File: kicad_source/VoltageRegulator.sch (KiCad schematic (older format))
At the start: 27 parts, among them P2 WR-TBL_691313710002, Q1 IPD90P03P4L- 04, U9 IFX91041EJV

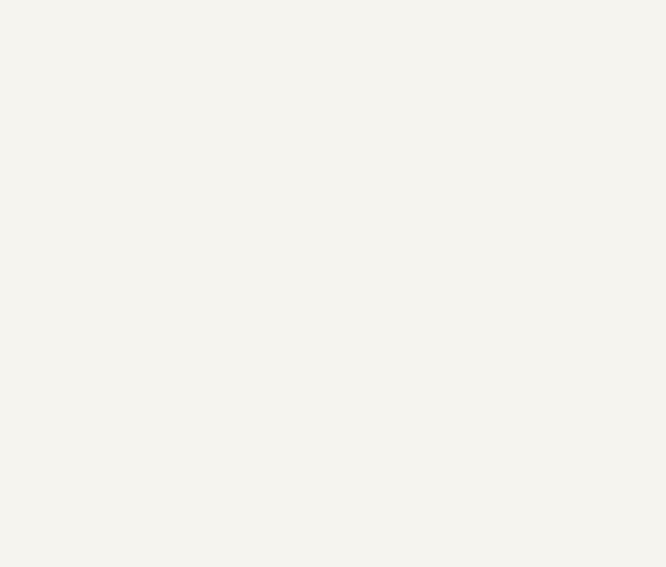
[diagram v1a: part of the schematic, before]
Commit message: added most missing 3d models, changed mounting holes to parts and generated step model
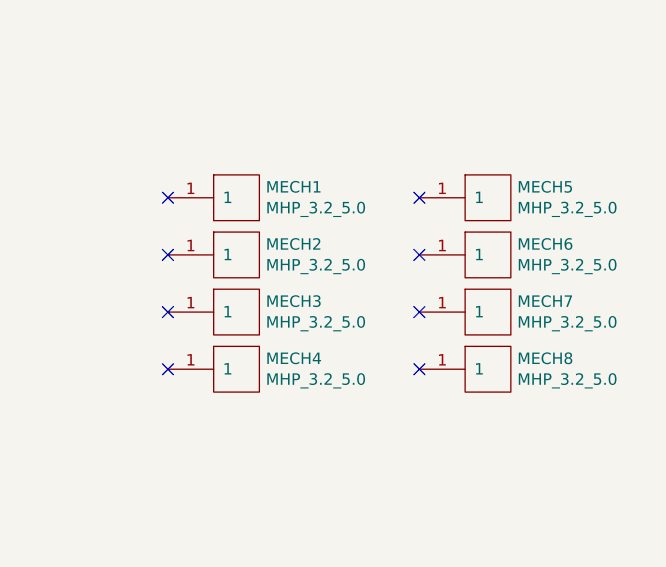
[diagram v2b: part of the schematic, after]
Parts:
- added MECH1, MECH2, MECH3, MECH4, MECH5, MECH6, MECH7, MECH8: MHP_3.2_5.0, MECH_mounting_holes:MHP_3.2_5.0, symbol MECH_mounting-holes:MHP_3.2_5.0
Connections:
- no-connect marks 0 -> 8
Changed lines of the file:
@@
 Text Label 4550 6450 0    60   ~ 0
 VIN_UNPOL
+$Comp
+L MECH_mounting-holes:MHP_3.2_5.0 MECH1
+U 1 1 5E994B25
+P 8550 5300
+F 0 "MECH1" H 8678 5346 50  0000 L CNN
+F 1 "MHP_3.2_5.0" H 8678 5255 50  0000 L CNN
+F 2 "MECH_mounting_holes:MHP_3.2_5.0" H 8450 5350 50  0001 C CNN
+F 3 "" H 8550 5300 50  0001 C CNN
+	1    8550 5300
+	1    0    0    -1
+$EndComp
+$Comp
+L MECH_mounting-holes:MHP_3.2_5.0 MECH2
+U 1 1 5E995892
+P 8550 5550
+F 0 "MECH2" H 8678 5596 50  0000 L CNN
+F 1 "MHP_3.2_5.0" H 8678 5505 50  0000 L CNN
+F 2 "MECH_mounting_holes:MHP_3.2_5.0" H 8450 5600 50  0001 C CNN
+F 3 "" H 8550 5550 50  0001 C CNN
+	1    8550 5550
+	1    0    0    -1
+$EndComp
+$Comp
+L MECH_mounting-holes:MHP_3.2_5.0 MECH3
+U 1 1 5E99663D
+P 8550 5800
+F 0 "MECH3" H 8678 5846 50  0000 L CNN
+F 1 "MHP_3.2_5.0" H 8678 5755 50  0000 L CNN
+F 2 "MECH_mounting_holes:MHP_3.2_5.0" H 8450 5850 50  0001 C CNN
+F 3 "" H 8550 5800 50  0001 C CNN
+	1    8550 5800
+	1    0    0    -1
+$EndComp
+$Comp
+L MECH_mounting-holes:MHP_3.2_5.0 MECH4
+U 1 1 5E996647
+P 8550 6050
+F 0 "MECH4" H 8678 6096 50  0000 L CNN
+F 1 "MHP_3.2_5.0" H 8678 6005 50  0000 L CNN
+F 2 "MECH_mounting_holes:MHP_3.2_5.0" H 8450 6100 50  0001 C CNN
+F 3 "" H 8550 6050 50  0001 C CNN
+	1    8550 6050
+	1    0    0    -1
+$EndComp
+NoConn ~ 8250 5300
+NoConn ~ 8250 5550
+NoConn ~ 8250 5800
+NoConn ~ 8250 6050
+$Comp
+L MECH_mounting-holes:MHP_3.2_5.0 MECH5
+U 1 1 5E9A368E
+P 9650 5300
+F 0 "MECH5" H 9778 5346 50  0000 L CNN
+F 1 "MHP_3.2_5.0" H 9778 5255 50  0000 L CNN
+F 2 "MECH_mounting_holes:MHP_3.2_5.0" H 9550 5350 50  0001 C CNN
+F 3 "" H 9650 5300 50  0001 C CNN
+	1    9650 5300
+	1    0    0    -1
+$EndComp
+$Comp
+L MECH_mounting-holes:MHP_3.2_5.0 MECH6
+U 1 1 5E9A3698
+P 9650 5550
+F 0 "MECH6" H 9778 5596 50  0000 L CNN
+F 1 "MHP_3.2_5.0" H 9778 5505 50  0000 L CNN
+F 2 "MECH_mounting_holes:MHP_3.2_5.0" H 9550 5600 50  0001 C CNN
+F 3 "" H 9650 5550 50  0001 C CNN
+	1    9650 5550
+	1    0    0    -1
+$EndComp
+$Comp
+L MECH_mounting-holes:MHP_3.2_5.0 MECH7
+U 1 1 5E9A36A2
+P 9650 5800
+F 0 "MECH7" H 9778 5846 50  0000 L CNN
+F 1 "MHP_3.2_5.0" H 9778 5755 50  0000 L CNN
+F 2 "MECH_mounting_holes:MHP_3.2_5.0" H 9550 5850 50  0001 C CNN
+F 3 "" H 9650 5800 50  0001 C CNN
+	1    9650 5800
+	1    0    0    -1
+$EndComp
+$Comp
+L MECH_mounting-holes:MHP_3.2_5.0 MECH8
+U 1 1 5E9A36AC
+P 9650 6050
+F 0 "MECH8" H 9778 6096 50  0000 L CNN
+F 1 "MHP_3.2_5.0" H 9778 6005 50  0000 L CNN
+F 2 "MECH_mounting_holes:MHP_3.2_5.0" H 9550 6100 50  0001 C CNN
+F 3 "" H 9650 6050 50  0001 C CNN
+	1    9650 6050
+	1    0    0    -1
+$EndComp
+NoConn ~ 9350 5300
+NoConn ~ 9350 5550
+NoConn ~ 9350 5800
+NoConn ~ 9350 6050
 $EndSCHEMATC

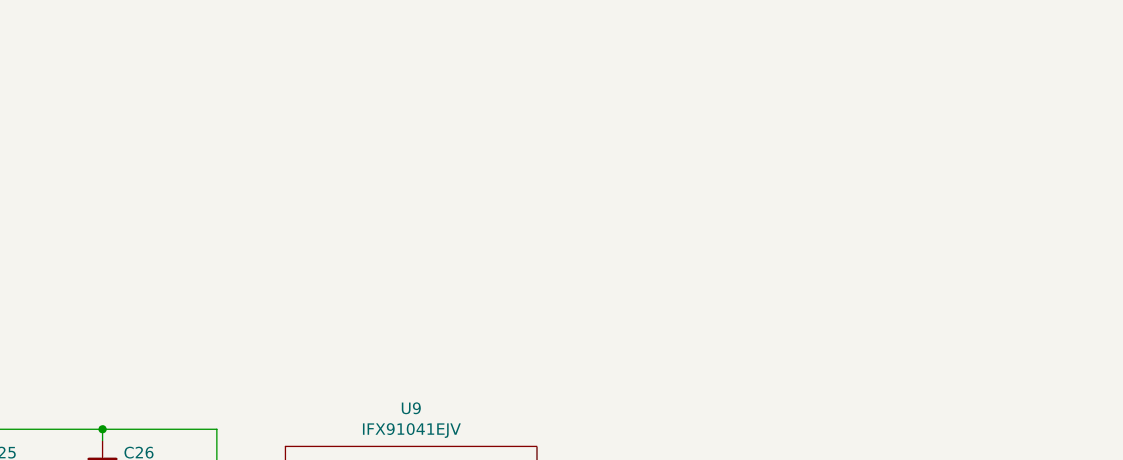
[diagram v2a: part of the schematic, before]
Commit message: added external supply for +5V for TMC5130
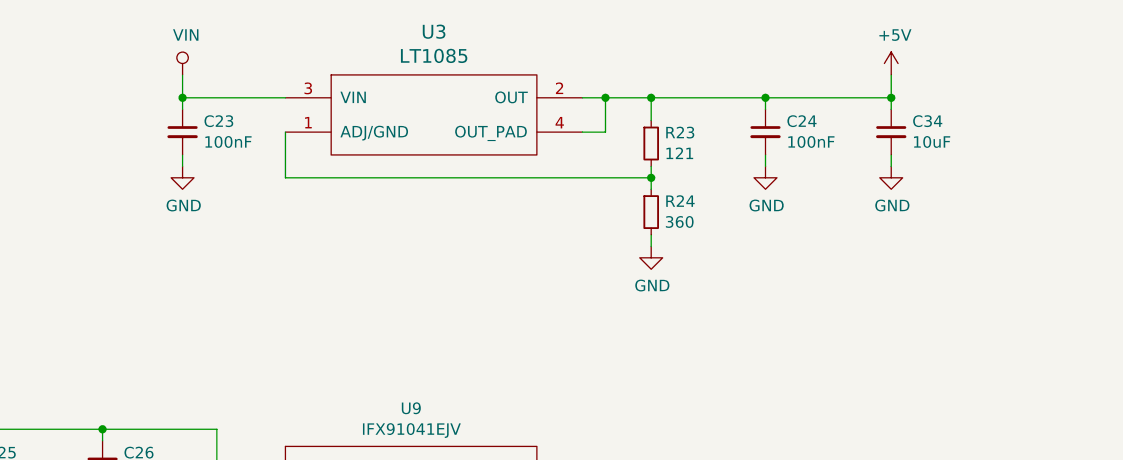
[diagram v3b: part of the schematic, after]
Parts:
- added C23, C24: 100nF, capacitors:C_0603, symbol devices:C_0603
- added C34: 10uF, capacitors:C_0805, symbol devices:C_0805
- added R23: 121, resistors:R_0603, symbol devices:R_0603
- added R24: 360, resistors:R_0603, symbol devices:R_0603
- added U3: LT1085, SOT_TO:TO-263-3Lead, symbol voltage-regulators:LT1085
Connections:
- net GND: now also C23.2, C24.2, C34.2, R24.2
- net VIN: now also C23.1, U3.3 (VIN)
- new net: R23.2, R24.1, U3.1 (ADJ/GND)
- new net +5V: C24.1, C34.1, R23.1, U3.2 (OUT), U3.4 (OUT_PAD)
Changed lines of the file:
@@
 NoConn ~ 9350 5800
 NoConn ~ 9350 6050
+$Comp
+L voltage-regulators:LT1085 U3
+U 1 1 5EFFCCD0
+P 5250 1750
+F 0 "U3" H 5250 2137 60  0000 C CNN
+F 1 "LT1085" H 5250 2031 60  0000 C CNN
+F 2 "SOT_TO:TO-263-3Lead" H 5200 1450 60  0001 C CNN
+F 3 "" H 5250 1750 60  0000 C CNN
+	1    5250 1750
+	1    0    0    -1
+$EndComp
+$Comp
+L devices:C_0603 C23
+U 1 1 5EFFFCEC
+P 4150 1800
+F 0 "C23" H 4242 1846 50  0000 L CNN
+F 1 "100nF" H 4242 1755 50  0000 L CNN
+F 2 "capacitors:C_0603" H 4150 1650 50  0001 C CNN
+F 3 "" H 4150 1800 50  0000 C CNN
+	1    4150 1800
+	1    0    0    -1
+$EndComp
+$Comp
+L devices:C_0603 C24
+U 1 1 5F000D88
+P 6700 1800
+F 0 "C24" H 6792 1846 50  0000 L CNN
+F 1 "100nF" H 6792 1755 50  0000 L CNN
+F 2 "capacitors:C_0603" H 6700 1650 50  0001 C CNN
+F 3 "" H 6700 1800 50  0000 C CNN
+	1    6700 1800
+	1    0    0    -1
+$EndComp
+$Comp
+L power-supply:+5V #PWR087
+U 1 1 5F001A73
+P 7250 1550
+F 0 "#PWR087" H 7250 1400 50  0001 C CNN
+F 1 "+5V" H 7265 1723 50  0000 C CNN
+F 2 "" H 7250 1550 50  0000 C CNN
+F 3 "" H 7250 1550 50  0000 C CNN
+	1    7250 1550
+	1    0    0    -1
+$EndComp
+$Comp
+L power-supply:GND #PWR023
+U 1 1 5F002420
+P 6700 1950
+F 0 "#PWR023" H 6700 1700 50  0001 C CNN
+F 1 "GND" H 6705 1777 50  0000 C CNN
+F 2 "" H 6700 1950 50  0000 C CNN
+F 3 "" H 6700 1950 50  0000 C CNN
+	1    6700 1950
+	1    0    0    -1
+$EndComp
+$Comp
+L power-supply:GND #PWR088
+U 1 1 5F002B69
+P 7250 1950
+F 0 "#PWR088" H 7250 1700 50  0001 C CNN
+F 1 "GND" H 7255 1777 50  0000 C CNN
+F 2 "" H 7250 1950 50  0000 C CNN
+F 3 "" H 7250 1950 50  0000 C CNN
+	1    7250 1950
+	1    0    0    -1
+$EndComp
+$Comp
+L devices:R_0603 R23
+U 1 1 5F003140
+P 6200 1850
+F 0 "R23" H 6259 1896 50  0000 L CNN
+F 1 "121" H 6259 1805 50  0000 L CNN
+F 2 "resistors:R_0603" H 6200 1700 50  0001 C CNN
+F 3 "" H 6200 1850 50  0000 C CNN
+	1    6200 1850
+	1    0    0    -1
+$EndComp
+$Comp
+L devices:R_0603 R24
+U 1 1 5F0037F9
+P 6200 2150
+F 0 "R24" H 6259 2196 50  0000 L CNN
+F 1 "360" H 6259 2105 50  0000 L CNN
+F 2 "resistors:R_0603" H 6200 2000 50  0001 C CNN
+F 3 "" H 6200 2150 50  0000 C CNN
+	1    6200 2150
+	1    0    0    -1
+$EndComp
+$Comp
+L power-supply:GND #PWR022
+U 1 1 5F003B9D
+P 6200 2300
+F 0 "#PWR022" H 6200 2050 50  0001 C CNN
+F 1 "GND" H 6205 2127 50  0000 C CNN
+F 2 "" H 6200 2300 50  0000 C CNN
+F 3 "" H 6200 2300 50  0000 C CNN
+	1    6200 2300
+	1    0    0    -1
+$EndComp
+$Comp
+L power-supply:GND #PWR019
+U 1 1 5F003E85
+P 4150 1950
+F 0 "#PWR019" H 4150 1700 50  0001 C CNN
+F 1 "GND" H 4155 1777 50  0000 C CNN
+F 2 "" H 4150 1950 50  0000 C CNN
+F 3 "" H 4150 1950 50  0000 C CNN
+	1    4150 1950
+	1    0    0    -1
+$EndComp
+$Comp
+L power-supply:VIN #PWR017
+U 1 1 5F00408E
+P 4150 1550
+F 0 "#PWR017" H 4150 1400 50  0001 C CNN
+F 1 "VIN" H 4167 1723 50  0000 C CNN
+F 2 "" H 4150 1550 50  0000 C CNN
+F 3 "" H 4150 1550 50  0000 C CNN
+	1    4150 1550
+	1    0    0    -1
+$EndComp
+$Comp
+L devices:C_0805 C34
+U 1 1 5F004CA8
+P 7250 1800
+F 0 "C34" H 7342 1846 50  0000 L CNN
+F 1 "10uF" H 7342 1755 50  0000 L CNN
+F 2 "capacitors:C_0805" H 7250 1650 50  0001 C CNN
+F 3 "" H 7250 1800 50  0000 C CNN
+	1    7250 1800
+	1    0    0    -1
+$EndComp
+Wire Wire Line
+	4150 1550 4150 1650
+Wire Wire Line
+	4150 1900 4150 1950
+Wire Wire Line
+	4600 1650 4150 1650
+Connection ~ 4150 1650
+Wire Wire Line
+	4150 1650 4150 1700
+Wire Wire Line
+	7250 1650 7250 1550
+Wire Wire Line
+	7250 1700 7250 1650
+Connection ~ 7250 1650
+Wire Wire Line
+	6700 1700 6700 1650
+Connection ~ 6700 1650
+Wire Wire Line
+	6700 1650 7250 1650
+Wire Wire Line
+	6200 1750 6200 1650
+Connection ~ 6200 1650
+Wire Wire Line
+	6200 1650 6700 1650
+Wire Wire Line
+	5900 1650 6000 1650
+Wire Wire Line
+	5900 1800 6000 1800
+Wire Wire Line
+	6000 1800 6000 1650
+Connection ~ 6000 1650
+Wire Wire Line
+	6000 1650 6200 1650
+Wire Wire Line
+	6200 1950 6200 2000
+Wire Wire Line
+	6700 1900 6700 1950
+Wire Wire Line
+	7250 1900 7250 1950
+Wire Wire Line
+	6200 2250 6200 2300
+Wire Wire Line
+	6200 2000 4600 2000
+Wire Wire Line
+	4600 2000 4600 1800
+Connection ~ 6200 2000
+Wire Wire Line
+	6200 2000 6200 2050
 $EndSCHEMATC

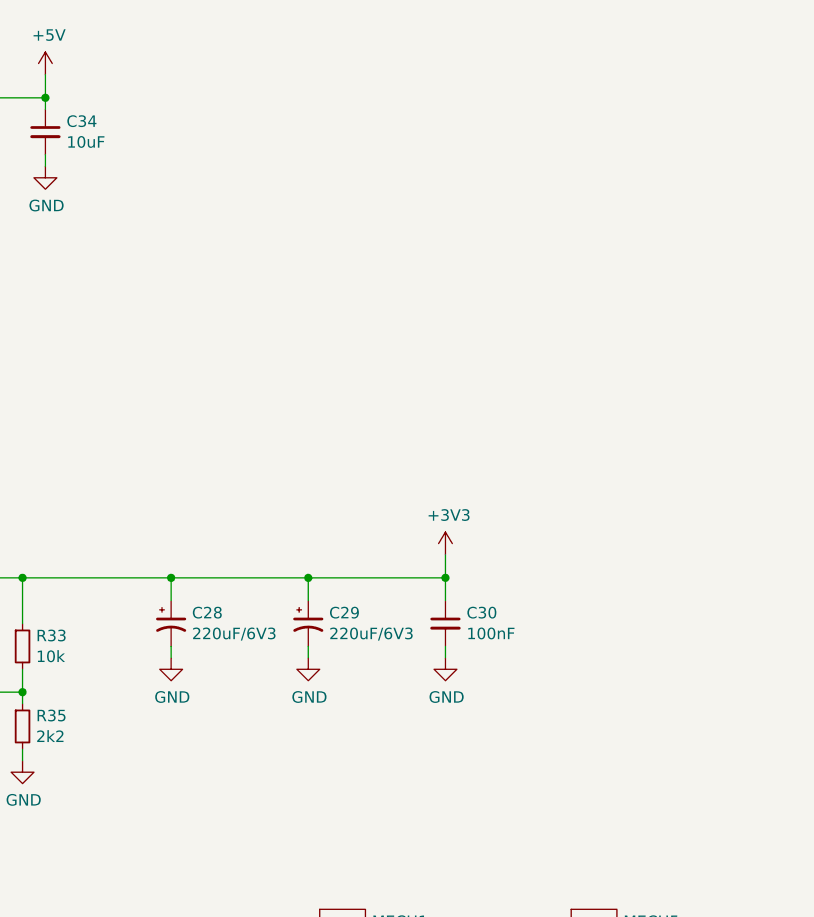
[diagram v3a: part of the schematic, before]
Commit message: added leds and decoupling capacitors
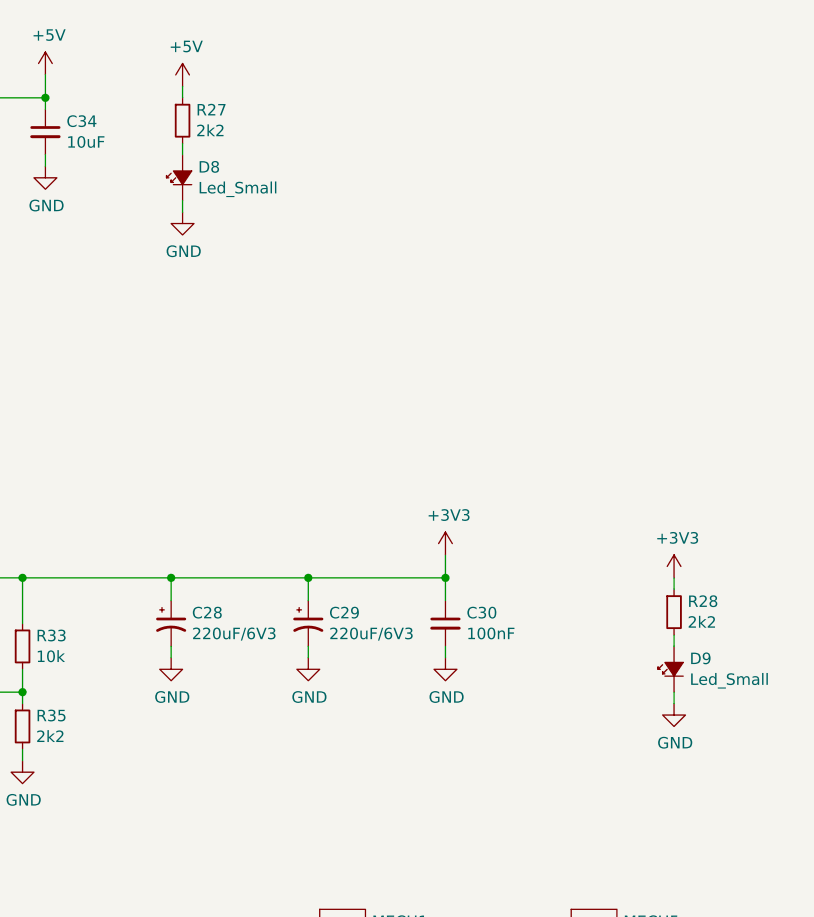
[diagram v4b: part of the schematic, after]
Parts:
- added D8, D9: Led_Small, LEDs:LED_0603, symbol devices:Led_Small
- added R27, R28: 2k2, resistors:R_0603, symbol devices:R_0603
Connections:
- net +3V3: now also R28.1
- net +5V: now also R27.1
- net GND: now also D8.1 (K), D9.1 (K)
- new net: D9.2 (A), R28.2
- new net: D8.2 (A), R27.2
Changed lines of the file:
@@
 Sheet 3 6
 Title "HighPowerMotorFeatherWing"
-Date "2019-12-31"
-Rev "1.0"
+Date "2020-07-04"
+Rev "1.1"
 Comp "generationmake"
 Comment1 ""
@@
 Wire Wire Line
 	6200 2000 6200 2050
+$Comp
+L devices:Led_Small D9
+U 1 1 5F0020ED
+P 10000 4150
+F 0 "D9" V 10046 4082 50  0000 R CNN
+F 1 "Led_Small" V 9955 4082 50  0000 R CNN
+F 2 "LEDs:LED_0603" V 10000 4150 50  0001 C CNN
+F 3 "" V 10000 4150 50  0000 C CNN
+	1    10000 4150
+	0    -1   -1   0
+$EndComp
+$Comp
+L devices:R_0603 R28
+U 1 1 5F002633
+P 10000 3900
+F 0 "R28" H 10059 3946 50  0000 L CNN
+F 1 "2k2" H 10059 3855 50  0000 L CNN
+F 2 "resistors:R_0603" H 10000 3750 50  0001 C CNN
+F 3 "" H 10000 3900 50  0000 C CNN
+	1    10000 3900
+	1    0    0    -1
+$EndComp
+$Comp
+L power-supply:+3V3 #PWR098
+U 1 1 5F002941
+P 10000 3750
+F 0 "#PWR098" H 10000 3600 50  0001 C CNN
+F 1 "+3V3" H 10015 3923 50  0000 C CNN
+F 2 "" H 10000 3750 50  0000 C CNN
+F 3 "" H 10000 3750 50  0000 C CNN
+	1    10000 3750
+	1    0    0    -1
+$EndComp
+$Comp
+L power-supply:GND #PWR099
+U 1 1 5F002C61
+P 10000 4300
+F 0 "#PWR099" H 10000 4050 50  0001 C CNN
+F 1 "GND" H 10005 4127 50  0000 C CNN
+F 2 "" H 10000 4300 50  0000 C CNN
+F 3 "" H 10000 4300 50  0000 C CNN
+	1    10000 4300
+	1    0    0    -1
+$EndComp
+Wire Wire Line
+	10000 3750 10000 3800
+Wire Wire Line
+	10000 4000 10000 4050
+Wire Wire Line
+	10000 4250 10000 4300
+$Comp
+L devices:Led_Small D8
+U 1 1 5F00E97E
+P 7850 2000
+F 0 "D8" V 7896 1932 50  0000 R CNN
+F 1 "Led_Small" V 7805 1932 50  0000 R CNN
+F 2 "LEDs:LED_0603" V 7850 2000 50  0001 C CNN
+F 3 "" V 7850 2000 50  0000 C CNN
+	1    7850 2000
+	0    -1   -1   0
+$EndComp
+$Comp
+L devices:R_0603 R27
+U 1 1 5F00E988
+P 7850 1750
+F 0 "R27" H 7909 1796 50  0000 L CNN
+F 1 "2k2" H 7909 1705 50  0000 L CNN
+F 2 "resistors:R_0603" H 7850 1600 50  0001 C CNN
+F 3 "" H 7850 1750 50  0000 C CNN
+	1    7850 1750
+	1    0    0    -1
+$EndComp
+$Comp
+L power-supply:GND #PWR025
+U 1 1 5F00E99C
+P 7850 2150
+F 0 "#PWR025" H 7850 1900 50  0001 C CNN
+F 1 "GND" H 7855 1977 50  0000 C CNN
+F 2 "" H 7850 2150 50  0000 C CNN
+F 3 "" H 7850 2150 50  0000 C CNN
+	1    7850 2150
+	1    0    0    -1
+$EndComp
+Wire Wire Line
+	7850 1600 7850 1650
+Wire Wire Line
+	7850 1850 7850 1900
+Wire Wire Line
+	7850 2100 7850 2150
+$Comp
+L power-supply:+5V #PWR024
+U 1 1 5F018DFC
+P 7850 1600
+F 0 "#PWR024" H 7850 1450 50  0001 C CNN
+F 1 "+5V" H 7865 1773 50  0000 C CNN
+F 2 "" H 7850 1600 50  0000 C CNN
+F 3 "" H 7850 1600 50  0000 C CNN
+	1    7850 1600
+	1    0    0    -1
+$EndComp
 $EndSCHEMATC

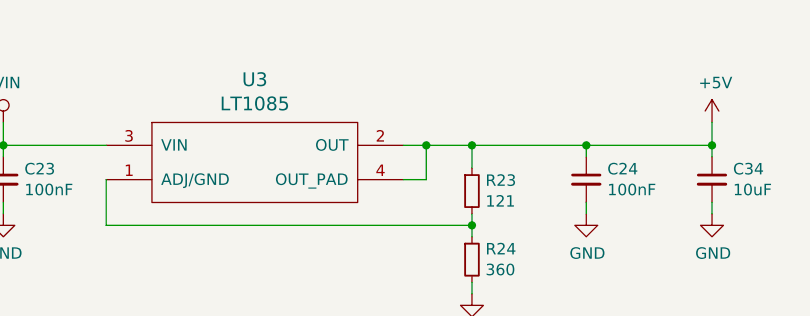
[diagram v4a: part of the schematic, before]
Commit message: added temperature sensor LM75
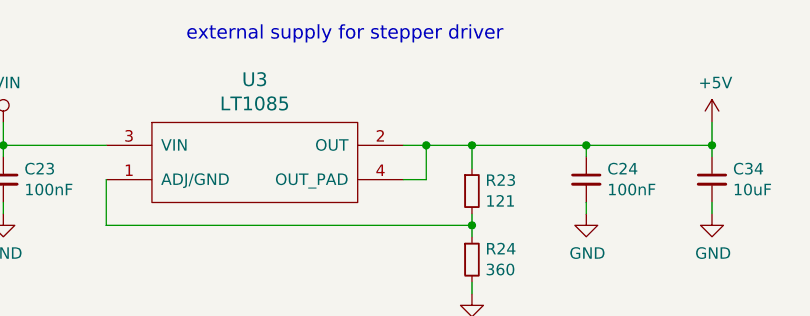
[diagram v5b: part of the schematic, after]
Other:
- note added: "external supply for stepper driver"
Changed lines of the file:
@@
 	1    0    0    -1
 $EndComp
+Text Notes 4950 1200 0    60   ~ 0
+external supply for stepper driver
 $EndSCHEMATC
